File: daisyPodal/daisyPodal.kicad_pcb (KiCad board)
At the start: 2 copper layers, 76 x 80 mm, 52 parts, among them J1 Guitar in, J2 fsw pin 1, J3 fsw pin 2, J4 fsw pin 4, J5 fsw pin 5, J6 fsw pin 6, J7 Left out, J8 Right out, J9 fsw pin 3, SW1 Switch 1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

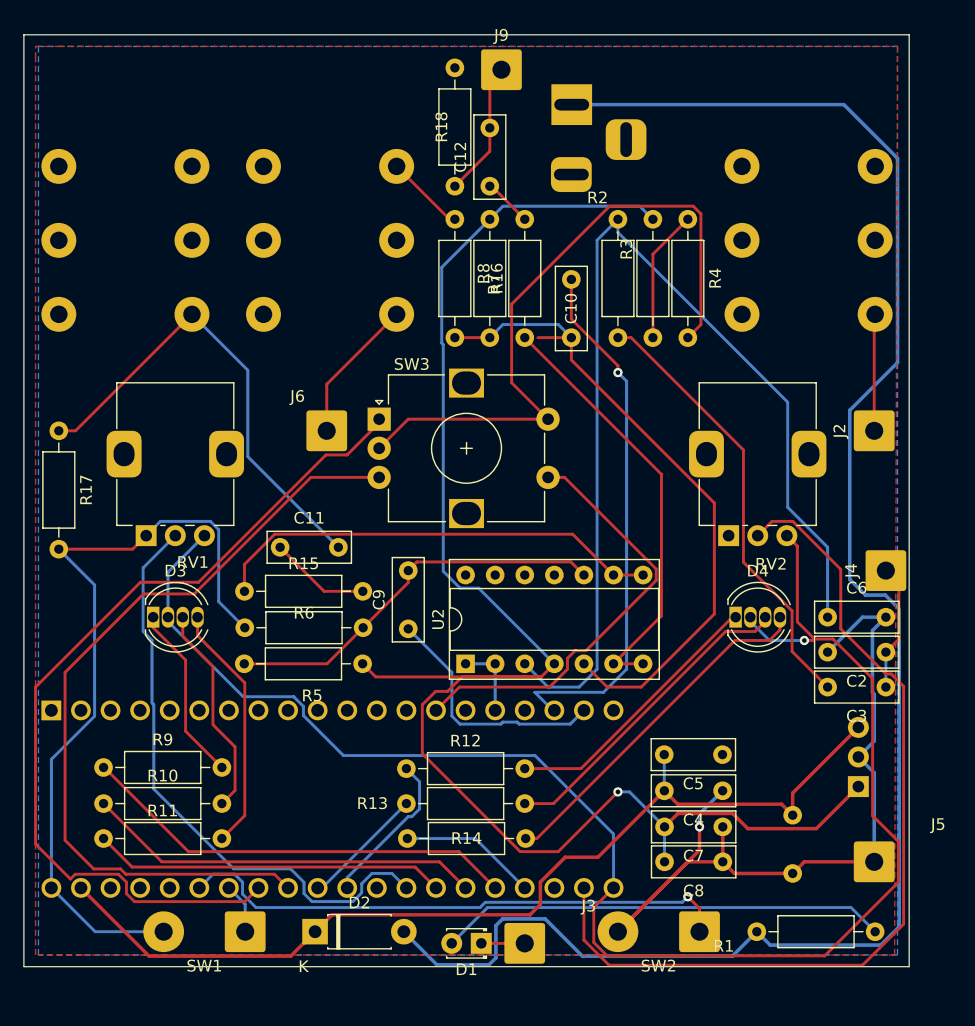
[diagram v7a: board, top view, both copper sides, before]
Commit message: Fix input buffer circuit and re-jig PCB
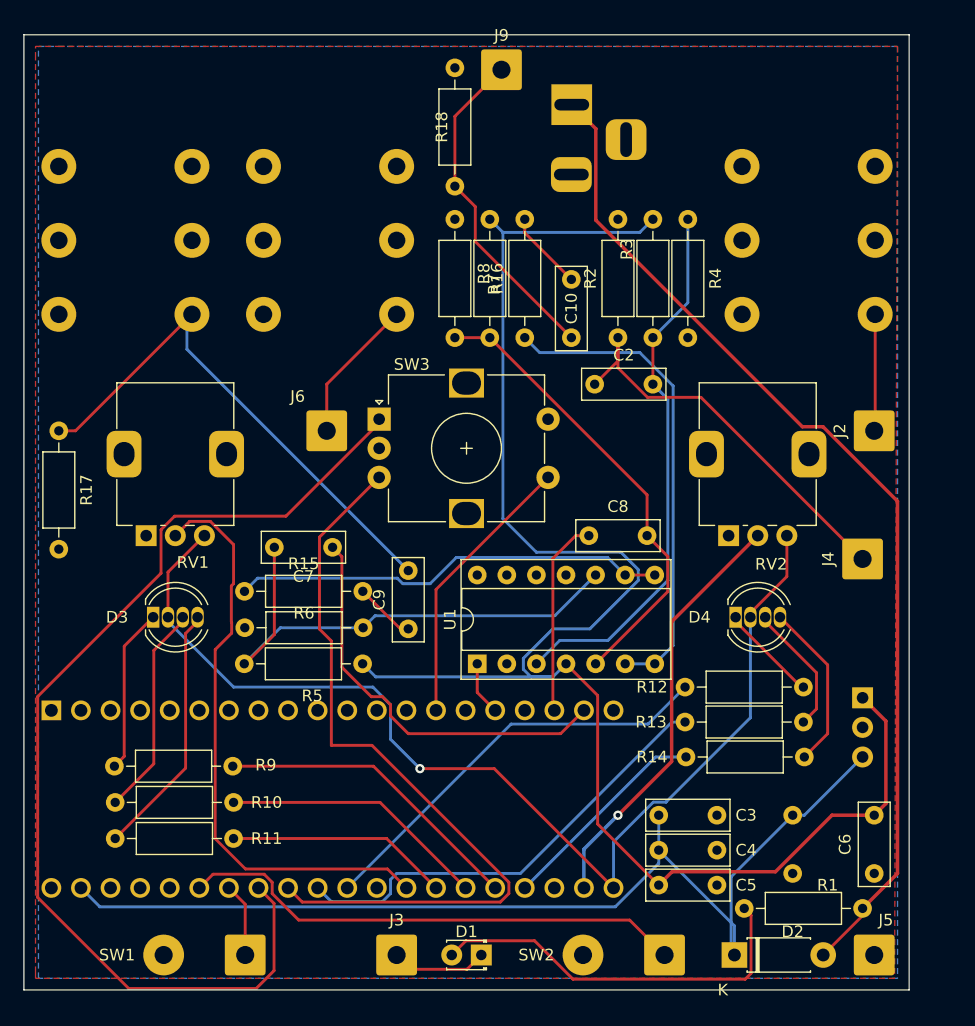
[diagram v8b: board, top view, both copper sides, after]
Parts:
- removed C11, C12: 1u, Capacitor_THT:C_Rect_L7.0mm_W2.5mm_P5.00mm
- C2: value 100p -> 1u
- C3: value 1u -> 100n
- C6: value 1n -> 100n
- C7, C8: value 100n -> 1u
- R2: value 1k -> 1M
- U1: value L78L05_TO92 -> TL074; footprint Package_TO_SOT_THT:TO-92_Inline_Wide_78L05_dc -> Package_DIP:DIP-14_W7.62mm_Socket; moved to F.Cu
- U2: value TL074 -> L78L05_TO92; footprint Package_DIP:DIP-14_W7.62mm_Socket -> Package_TO_SOT_THT:TO-92_Inline_Wide_78L05_dc; moved to B.Cu
- moved C7 41.2 mm to (125.5, 96.0)
- moved D2 36.1 mm to (160.0, 131.0)
- moved U1 34.4 mm to (137.9, 106.0)
- moved U2 34.2 mm to (171.0, 108.9), turned to -90 degrees
- moved C2 34.0 mm to (148.0, 82.0), turned to 0 degrees
- moved C8 30.3 mm to (147.5, 95.0), turned to 0 degrees
- moved R14 24.9 mm to (155.8, 114.0)
- moved R12 24.9 mm to (155.8, 108.0)
- moved R13 24.9 mm to (155.8, 111.0)
- moved C6 22.4 mm to (172.0, 124.0), turned to 90 degrees
- moved C3 18.2 mm to (158.5, 119.0)
- moved C5 11.2 mm to (158.5, 125.0)
- moved R10 11.2 mm to (117.0, 117.9), turned to 180 degrees
- moved R11 11.2 mm to (117.0, 121.0), turned to 180 degrees
- moved R9 11.1 mm to (116.9, 114.8), turned to 180 degrees
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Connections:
- C10 pad 1: /Left out -> Net-(C10-Pad1)
- C10 pad 2: Net-(U2B-+) -> Net-(J9-Pin_1)
- C2 pad 2: GND -> Net-(U1A-+)
- C3 pad 1: Net-(J4-Pin_1) -> GND
- C3 pad 2: Net-(C3-Pad2) -> /VCC
- C5 pad 2: /VCC -> +5V
- C6 pad 1: Net-(U2A-+) -> GND
- C6 pad 2: GND -> +5V
- C7 pad 1: GND -> /Right out
- C7 pad 2: +5V -> Net-(U1C-+)
- C8 pad 1: GND -> /Left out
- C8 pad 2: +5V -> Net-(U1B-+)
- C9 pad 1: /Right out -> Net-(C9-Pad1)
- C9 pad 2: Net-(U2C-+) -> Net-(C9-Pad2)
- J8 pad T: Net-(C11-Pad2) -> Net-(C9-Pad2)
- R15 pad 1: Net-(U2C--) -> Net-(U1C--)
- R15 pad 2: Net-(C11-Pad1) -> Net-(C9-Pad1)
- R16 pad 1: Net-(U2B--) -> Net-(U1B--)
- R16 pad 2: Net-(C12-Pad1) -> Net-(C10-Pad1)
- R17 pad 1: Net-(C11-Pad2) -> Net-(C9-Pad2)
- R2 pad 1: Net-(C3-Pad2) -> Net-(J4-Pin_1)
- R2 pad 2: Net-(U2A-+) -> GND
- R3 pad 2: Net-(R3-Pad2) -> Net-(U1A-+)
- R4 pad 1: Net-(R3-Pad2) -> Net-(U1A-+)
- R5 pad 2: Net-(U2C-+) -> Net-(U1C-+)
- R6 pad 1: Net-(U2C-+) -> Net-(U1C-+)
- R7 pad 2: Net-(U2B-+) -> Net-(U1B-+)
- R8 pad 1: Net-(U2B-+) -> Net-(U1B-+)
- U1 pad 1: +5V -> /Left in
- U1 pad 2: GND -> unconnected-(U1A---Pad2)
- U1 pad 3: /VCC -> Net-(U1A-+)
- U2 pad 1: /Left in -> +5V
- U2 pad 2: /Left in -> GND
- U2 pad 3: Net-(U2A-+) -> /VCC
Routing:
- net GND: track 205.4 -> 0.00 mm, vias 1 -> 0
- net Net-(U2A-+): track 88.7 -> 0.00 mm
- net Net-(BT1-+): track 150.6 -> 88.3 mm
- net Net-(U2B-+): track 57.2 -> 0.00 mm
- net Net-(U1A-+): track 0.00 -> 47.2 mm
- net Net-(C9-Pad2): track 0.00 -> 45.9 mm
- net Net-(U1C-+): track 0.00 -> 44.4 mm
- net Net-(U1B--): track 0.00 -> 41.5 mm
- net Net-(C11-Pad2): track 40.8 -> 0.00 mm
- net /3v3: track 135.4 -> 95.2 mm
- net Net-(A1-ADC_0): track 76.6 -> 36.4 mm, vias 0 -> 1
- net Net-(U1B-+): track 0.00 -> 39.9 mm
- net Net-(U2C--): track 39.1 -> 0.00 mm
- net Net-(C3-Pad2): track 38.1 -> 0.00 mm
- net Net-(U1C--): track 0.00 -> 37.4 mm
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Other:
- board size 76 x 80 mm -> 76 x 82 mm
